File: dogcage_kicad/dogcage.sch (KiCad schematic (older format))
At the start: 10 parts, among them CON1 BARREL_JACK, M1 XBEE, P1 Servo, P2 Door Sensor, Q1 TIP120, SW1 SW_PUSH, U1 TEENSYLC, U2 LD1117S33TR

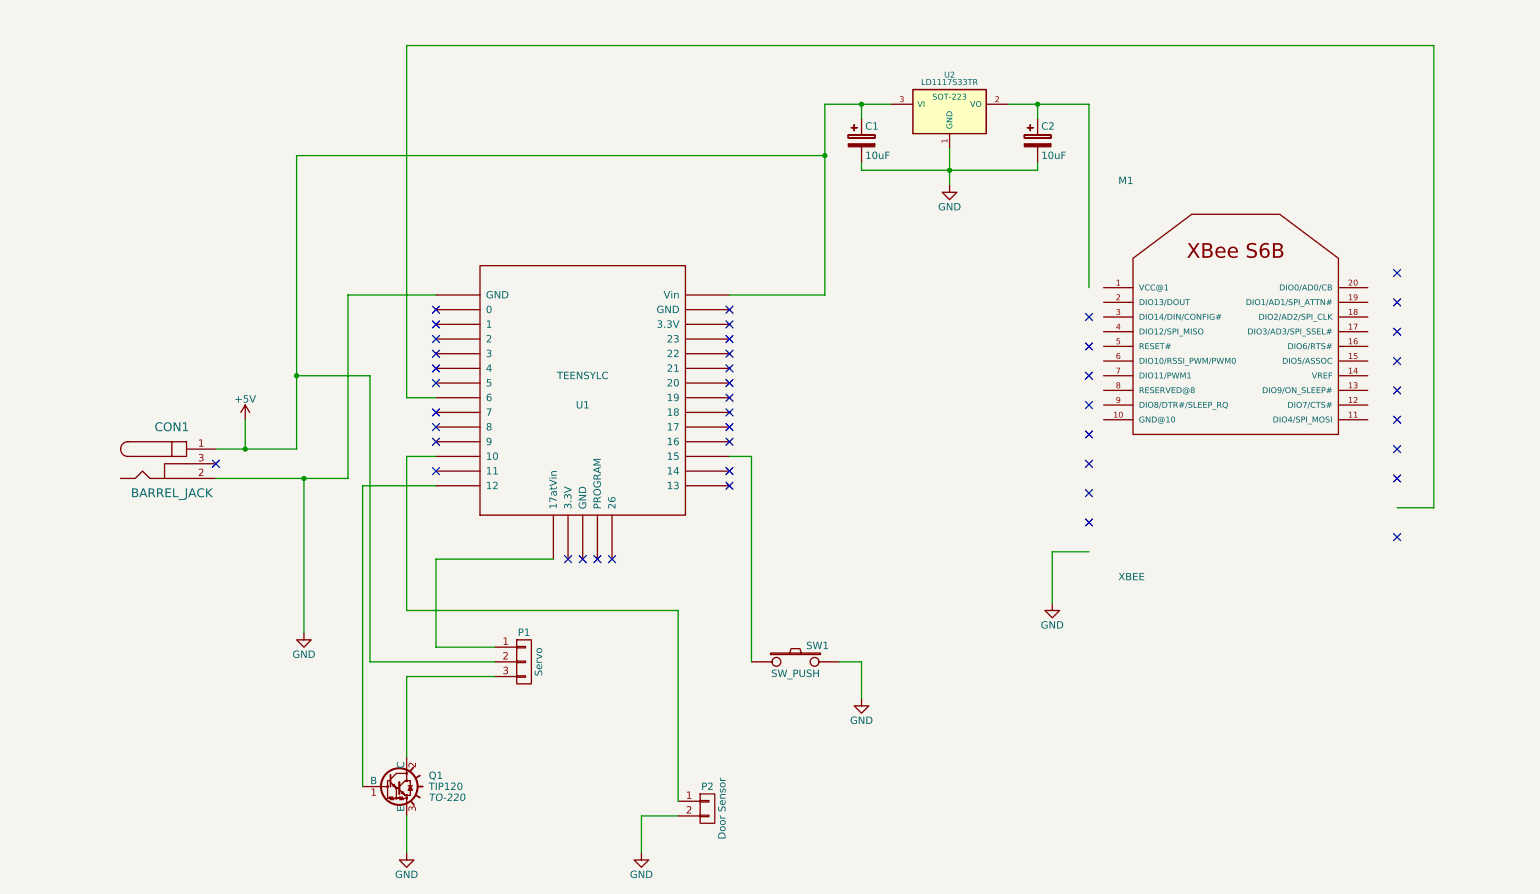
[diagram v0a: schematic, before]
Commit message: Cleaned up schematic and fixed ERC errors
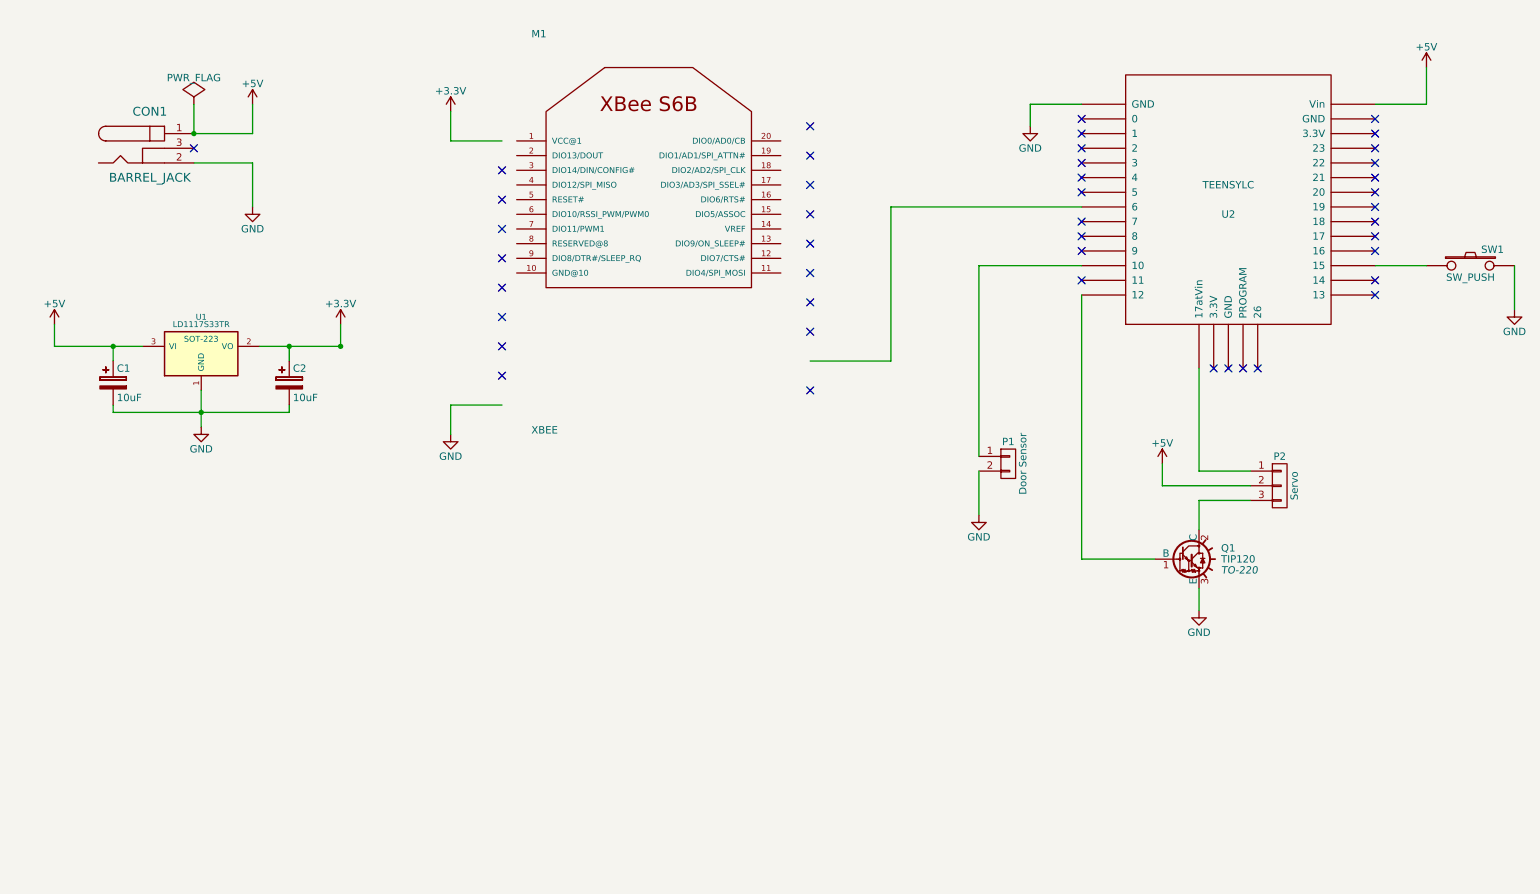
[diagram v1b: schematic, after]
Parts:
- renumbered P2 to P1, P1 to P2, U2 to U1, U1 to U2
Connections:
- net labels added: +3.3V
- wire segments 47 -> 40
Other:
- moved on the sheet: C1, C2, CON1, M1, P1, P2, Q1, SW1, U1, U2

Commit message: Added assoc LED and started on PCB
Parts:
- added D1: Assoc LED, symbol LED
- added R1: 330, symbol R
- CON1: footprint (none) -> Connect:BARREL_JACK
- P1: footprint (none) -> Pin_Headers:Pin_Header_Straight_1x02
- P2: footprint (none) -> Pin_Headers:Pin_Header_Straight_1x03
- Q1: footprint TO-220 -> Power_Integrations:TO-220
- SW1: footprint (none) -> Buttons_Switches_ThroughHole:SW_PUSH
- U1: footprint SOT-223 -> SMD_Packages:SOT-223
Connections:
- wire segments 40 -> 44
- no-connect marks 44 -> 43
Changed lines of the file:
@@
 F 0 "CON1" H 1550 1900 60  0000 C CNN
 F 1 "BARREL_JACK" H 1550 1450 60  0000 C CNN
-F 2 "" H 1550 1650 60  0000 C CNN
+F 2 "Connect:BARREL_JACK" H 1550 1650 60  0001 C CNN
 F 3 "" H 1550 1650 60  0000 C CNN
 	1    1550 1650
@@
 $EndComp
 $Comp
-L GND #PWR01
+L GND #PWR4
 U 1 1 553C44F5
 P 2250 2050
-F 0 "#PWR01" H 2250 1800 50  0001 C CNN
+F 0 "#PWR4" H 2250 1800 50  0001 C CNN
 F 1 "GND" H 2250 1900 50  0000 C CNN
 F 2 "" H 2250 2050 60  0000 C CNN
@@
 F 0 "P2" H 9250 4150 50  0000 C CNN
 F 1 "Servo" V 9350 3950 50  0000 C CNN
-F 2 "" H 9250 3950 60  0000 C CNN
+F 2 "Pin_Headers:Pin_Header_Straight_1x03" H 9250 3950 60  0001 C CNN
 F 3 "" H 9250 3950 60  0000 C CNN
 	1    9250 3950
@@
 $EndComp
 $Comp
-L GND #PWR02
+L GND #PWR12
 U 1 1 553C464F
 P 8700 4800
-F 0 "#PWR02" H 8700 4550 50  0001 C CNN
+F 0 "#PWR12" H 8700 4550 50  0001 C CNN
 F 1 "GND" H 8700 4650 50  0000 C CNN
 F 2 "" H 8700 4800 60  0000 C CNN
@@
 F 0 "SW1" H 10700 2560 50  0000 C CNN
 F 1 "SW_PUSH" H 10550 2370 50  0000 C CNN
-F 2 "" H 10550 2450 60  0000 C CNN
+F 2 "Buttons_Switches_ThroughHole:SW_PUSH" H 10550 2450 60  0001 C CNN
 F 3 "" H 10550 2450 60  0000 C CNN
 	1    10550 2450
@@
 	9900 2450 10250 2450
 $Comp
-L GND #PWR03
+L GND #PWR14
 U 1 1 553C47AE
 P 10850 2750
-F 0 "#PWR03" H 10850 2500 50  0001 C CNN
+F 0 "#PWR14" H 10850 2500 50  0001 C CNN
 F 1 "GND" H 10850 2600 50  0000 C CNN
 F 2 "" H 10850 2750 60  0000 C CNN
@@
 F 0 "P1" H 7400 3950 50  0000 C CNN
 F 1 "Door Sensor" V 7500 3800 50  0000 C CNN
-F 2 "" H 7400 3800 60  0000 C CNN
+F 2 "Pin_Headers:Pin_Header_Straight_1x02" H 7400 3800 60  0001 C CNN
 F 3 "" H 7400 3800 60  0000 C CNN
 	1    7400 3800
@@
 	7200 2450 7900 2450
 $Comp
-L GND #PWR04
+L GND #PWR9
 U 1 1 553C48BE
 P 7200 4150
-F 0 "#PWR04" H 7200 3900 50  0001 C CNN
+F 0 "#PWR9" H 7200 3900 50  0001 C CNN
 F 1 "GND" H 7200 4000 50  0000 C CNN
 F 2 "" H 7200 4150 60  0000 C CNN
@@
 F 0 "Q1" H 8850 4525 50  0000 L CNN
 F 1 "TIP120" H 8850 4450 50  0000 L CNN
-F 2 "TO-220" H 8850 4375 50  0000 L CIN
+F 2 "Power_Integrations:TO-220" H 8850 4375 50  0000 L CIN
 F 3 "" H 8600 4450 50  0000 L CNN
 	1    8600 4450
@@
 $EndComp
 $Comp
-L GND #PWR05
+L GND #PWR7
 U 1 1 553C50DC
 P 3600 3600
-F 0 "#PWR05" H 3600 3350 50  0001 C CNN
+F 0 "#PWR7" H 3600 3350 50  0001 C CNN
 F 1 "GND" H 3600 3450 50  0000 C CNN
 F 2 "" H 3600 3600 60  0000 C CNN
@@
 NoConn ~ 6050 2100
 NoConn ~ 6050 2300
-NoConn ~ 6050 2500
 NoConn ~ 6050 2700
 NoConn ~ 6050 2900
@@
 F 0 "U1" H 1900 3300 40  0000 C CNN
 F 1 "LD1117S33TR" H 1900 3250 40  0000 C CNN
-F 2 "SOT-223" H 1900 3150 40  0000 C CNN
+F 2 "SMD_Packages:SOT-223" H 1900 3150 40  0000 C CNN
 F 3 "" H 1900 3050 60  0000 C CNN
 	1    1900 3050
@@
 	2850 3000 2850 2850
 $Comp
-L GND #PWR06
+L GND #PWR2
 U 1 1 553C52E7
 P 1900 3550
-F 0 "#PWR06" H 1900 3300 50  0001 C CNN
+F 0 "#PWR2" H 1900 3300 50  0001 C CNN
 F 1 "GND" H 1900 3400 50  0000 C CNN
 F 2 "" H 1900 3550 60  0000 C CNN
@@
 F 0 "C1" H 1325 3350 50  0000 L CNN
 F 1 "10uF" H 1325 3150 50  0000 L CNN
-F 2 "" H 1338 3100 30  0000 C CNN
+F 2 "" H 1338 3100 30  0001 C CNN
 F 3 "" H 1300 3250 60  0000 C CNN
 	1    1300 3250
@@
 F 0 "C2" H 2525 3350 50  0000 L CNN
 F 1 "10uF" H 2525 3150 50  0000 L CNN
-F 2 "" H 2538 3100 30  0000 C CNN
+F 2 "" H 2538 3100 30  0001 C CNN
 F 3 "" H 2500 3250 60  0000 C CNN
 	1    2500 3250
@@
 Connection ~ 2500 3000
 $Comp
-L PWR_FLAG #FLG07
+L PWR_FLAG #FLG1
 U 1 1 553C5BFF
 P 1850 1350
-F 0 "#FLG07" H 1850 1445 50  0001 C CNN
+F 0 "#FLG1" H 1850 1445 50  0001 C CNN
 F 1 "PWR_FLAG" H 1850 1530 50  0000 C CNN
 F 2 "" H 1850 1350 60  0000 C CNN
@@
 	2250 1750 2250 2050
 $Comp
-L +5V #PWR08
+L +5V #PWR3
 U 1 1 553C5EEA
 P 2250 1350
-F 0 "#PWR08" H 2250 1200 50  0001 C CNN
+F 0 "#PWR3" H 2250 1200 50  0001 C CNN
 F 1 "+5V" H 2250 1490 50  0000 C CNN
 F 2 "" H 2250 1350 60  0000 C CNN
@@
 	2250 1550 2250 1350
 $Comp
-L +5V #PWR09
+L +5V #PWR11
 U 1 1 553C5FA1
 P 8450 3800
-F 0 "#PWR09" H 8450 3650 50  0001 C CNN
+F 0 "#PWR11" H 8450 3650 50  0001 C CNN
 F 1 "+5V" H 8450 3940 50  0000 C CNN
 F 2 "" H 8450 3800 60  0000 C CNN
@@
 	8450 3950 9050 3950
 $Comp
-L GND #PWR010
+L GND #PWR10
 U 1 1 553C6094
 P 7550 1500
-F 0 "#PWR010" H 7550 1250 50  0001 C CNN
+F 0 "#PWR10" H 7550 1250 50  0001 C CNN
 F 1 "GND" H 7550 1350 50  0000 C CNN
 F 2 "" H 7550 1500 60  0000 C CNN
@@
 	7550 1350 7550 1500
 $Comp
-L +5V #PWR011
+L +5V #PWR13
 U 1 1 553C6264
 P 10250 1100
-F 0 "#PWR011" H 10250 950 50  0001 C CNN
+F 0 "#PWR13" H 10250 950 50  0001 C CNN
 F 1 "+5V" H 10250 1240 50  0000 C CNN
 F 2 "" H 10250 1100 60  0000 C CNN
@@
 	10250 1350 9900 1350
 $Comp
-L +5V #PWR012
+L +5V #PWR1
 U 1 1 553C62D3
 P 900 2850
-F 0 "#PWR012" H 900 2700 50  0001 C CNN
+F 0 "#PWR1" H 900 2700 50  0001 C CNN
 F 1 "+5V" H 900 2990 50  0000 C CNN
 F 2 "" H 900 2850 60  0000 C CNN
@@
 Connection ~ 1300 3000
 $Comp
-L +3.3V #PWR013
+L +3.3V #PWR5
 U 1 1 553C6392
 P 2850 2850
-F 0 "#PWR013" H 2850 2700 50  0001 C CNN
+F 0 "#PWR5" H 2850 2700 50  0001 C CNN
 F 1 "+3.3V" H 2850 2990 50  0000 C CNN
 F 2 "" H 2850 2850 60  0000 C CNN
@@
 	7900 4450 8400 4450
 $Comp
-L +3.3V #PWR014
+L +3.3V #PWR6
 U 1 1 553C783D
 P 3600 1400
-F 0 "#PWR014" H 3600 1250 50  0001 C CNN
+F 0 "#PWR6" H 3600 1250 50  0001 C CNN
 F 1 "+3.3V" H 3600 1540 50  0000 C CNN
 F 2 "" H 3600 1400 60  0000 C CNN
@@
 Wire Wire Line
 	6600 2050 7900 2050
+$Comp
+L LED D1
+U 1 1 553D18EC
+P 6300 3900
+F 0 "D1" H 6300 4000 50  0000 C CNN
+F 1 "Assoc LED" H 6300 3800 50  0000 C CNN
+F 2 "" H 6300 3900 60  0000 C CNN
+F 3 "" H 6300 3900 60  0000 C CNN
+	1    6300 3900
+	0    1    1    0
+$EndComp
+$Comp
+L GND #PWR8
+U 1 1 553D1931
+P 6300 4150
+F 0 "#PWR8" H 6300 3900 50  0001 C CNN
+F 1 "GND" H 6300 4000 50  0000 C CNN
+F 2 "" H 6300 4150 60  0000 C CNN
+F 3 "" H 6300 4150 60  0000 C CNN
+	1    6300 4150
+	1    0    0    -1
+$EndComp
+$Comp
+L R R1
+U 1 1 553D19C7
+P 6300 3450
+F 0 "R1" V 6380 3450 50  0000 C CNN
+F 1 "330" V 6300 3450 50  0000 C CNN
+F 2 "" V 6230 3450 30  0000 C CNN
+F 3 "" H 6300 3450 30  0000 C CNN
+	1    6300 3450
+	1    0    0    -1
+$EndComp
+Wire Wire Line
+	6300 4150 6300 4100
+Wire Wire Line
+	6300 3600 6300 3700
+Wire Wire Line
+	6050 2500 6300 2500
+Wire Wire Line
+	6300 2500 6300 3300
 $EndSCHEMATC

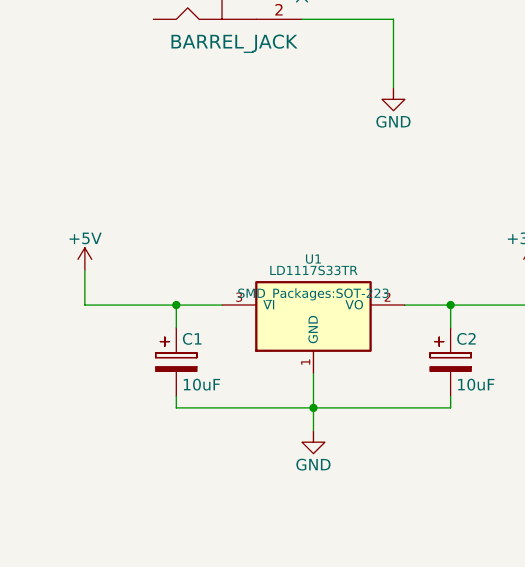
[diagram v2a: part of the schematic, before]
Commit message: Add protection diode to input power line
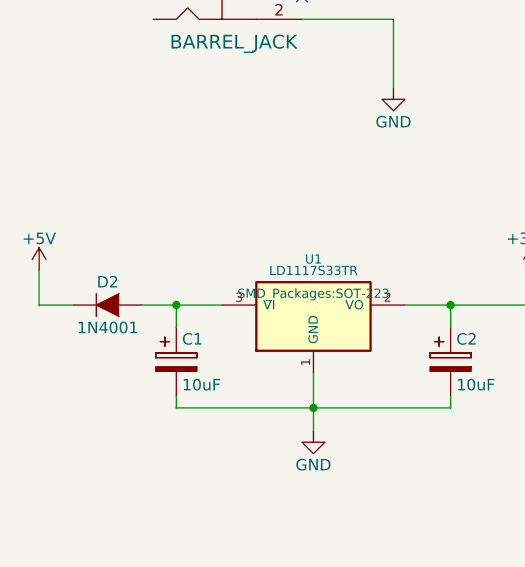
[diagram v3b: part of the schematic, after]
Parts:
- added D2: 1N4001, symbol D
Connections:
- wire segments 44 -> 45
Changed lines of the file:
@@
 $EndComp
 Wire Wire Line
-	900  3000 1500 3000
+	1150 3000 1500 3000
 Wire Wire Line
 	2300 3000 2850 3000
@@
 	2500 3450 2500 3400
 Wire Wire Line
-	1300 3100 1300 3000
+	1300 3000 1300 3100
 Wire Wire Line
 	2500 3100 2500 3000
@@
 L +5V #PWR1
 U 1 1 553C62D3
-P 900 2850
-F 0 "#PWR1" H 900 2700 50  0001 C CNN
-F 1 "+5V" H 900 2990 50  0000 C CNN
-F 2 "" H 900 2850 60  0000 C CNN
-F 3 "" H 900 2850 60  0000 C CNN
-	1    900  2850
-	1    0    0    -1
-$EndComp
-Wire Wire Line
-	900  2850 900  3000
+P 700 2850
+F 0 "#PWR1" H 700 2700 50  0001 C CNN
+F 1 "+5V" H 700 2990 50  0000 C CNN
+F 2 "" H 700 2850 60  0000 C CNN
+F 3 "" H 700 2850 60  0000 C CNN
+	1    700  2850
+	1    0    0    -1
+$EndComp
 Connection ~ 1300 3000
 $Comp
@@
 Wire Wire Line
 	6300 2500 6300 3300
+$Comp
+L D D2
+U 1 1 5541A2D5
+P 1000 3000
+F 0 "D2" H 1000 3100 50  0000 C CNN
+F 1 "1N4001" H 1000 2900 50  0000 C CNN
+F 2 "" H 1000 3000 60  0000 C CNN
+F 3 "" H 1000 3000 60  0000 C CNN
+	1    1000 3000
+	1    0    0    -1
+$EndComp
+Wire Wire Line
+	700  2850 700  3000
+Wire Wire Line
+	700  3000 850  3000
 $EndSCHEMATC

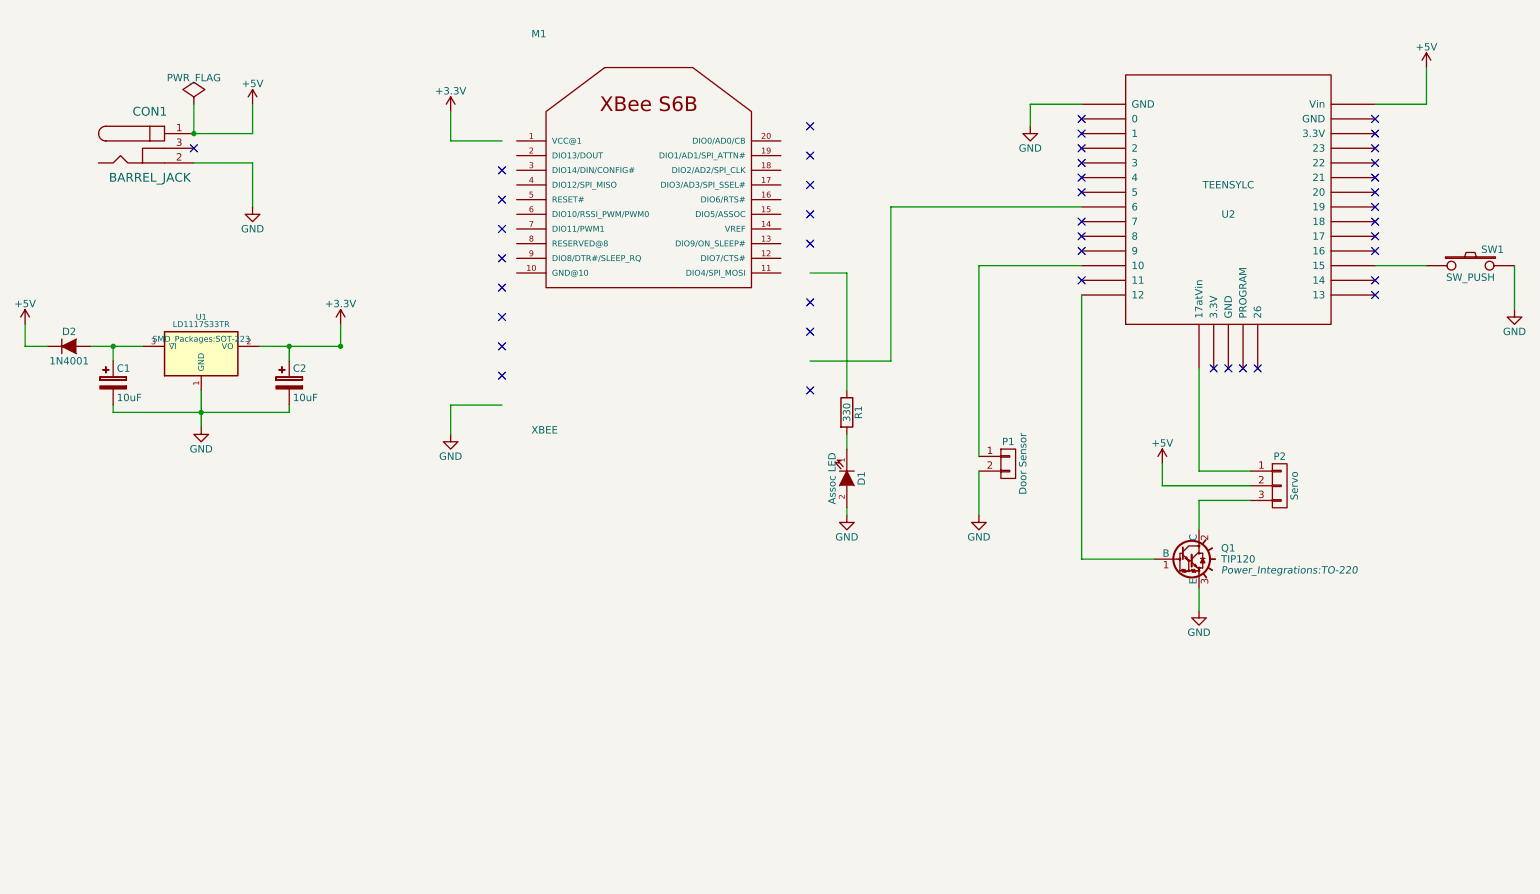
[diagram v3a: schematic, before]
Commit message: Added connectors to XBee and Teensy
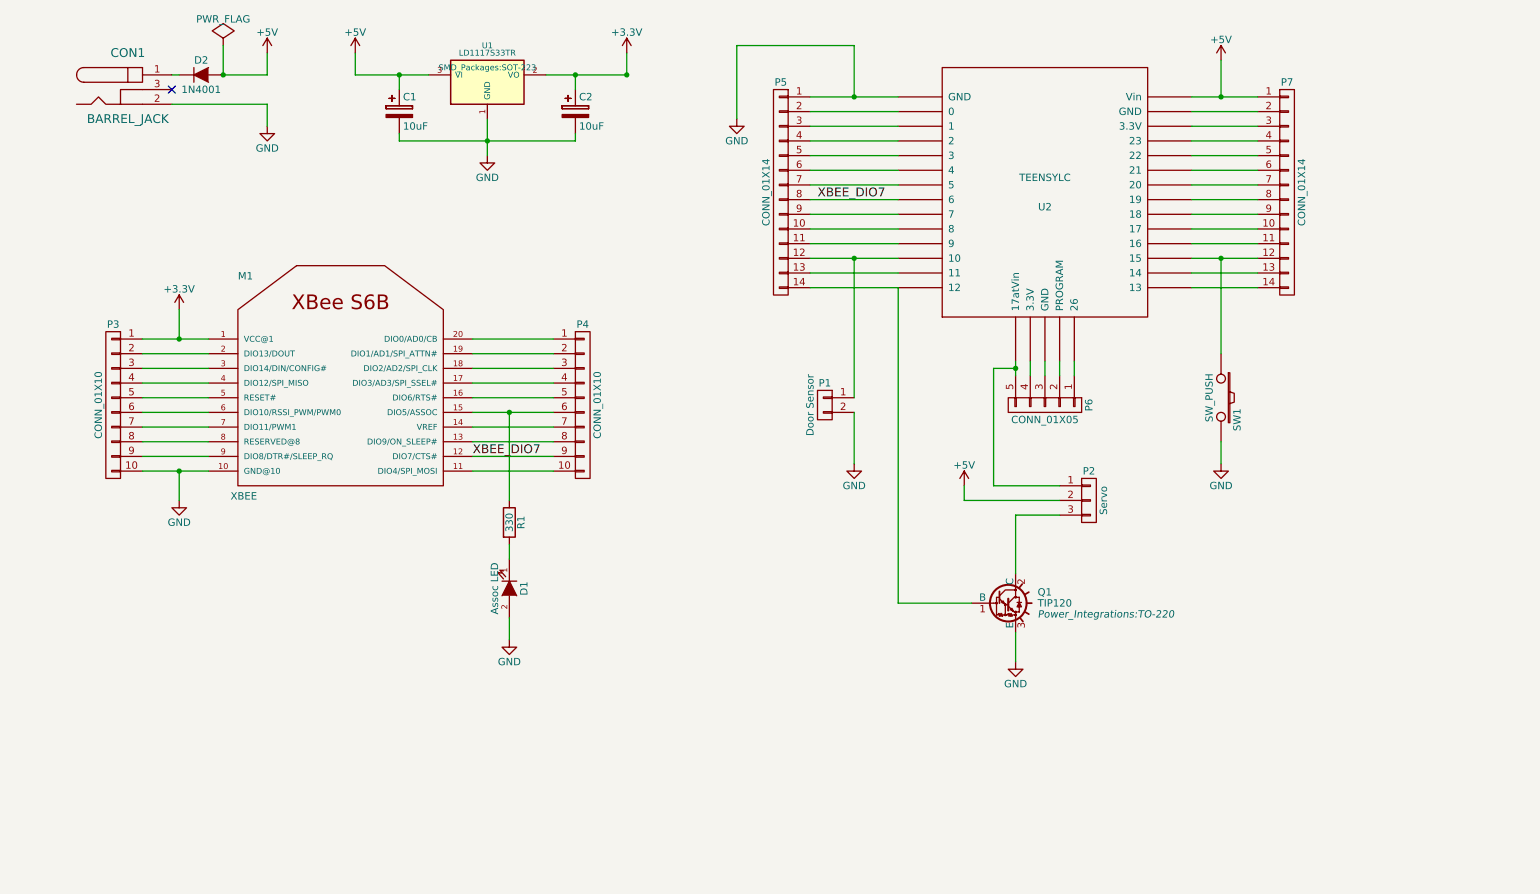
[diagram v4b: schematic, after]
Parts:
- added P3, P4: CONN_01X10, symbol CONN_01X10
- added P5, P7: CONN_01X14, symbol CONN_01X14
- added P6: CONN_01X05, symbol CONN_01X05
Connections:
- net labels added: XBEE_DIO7
- wire segments 45 -> 92
- no-connect marks 43 -> 1
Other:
- moved on the sheet: C1, C2, CON1, D1, D2, P1, P2, Q1, R1, SW1, U1, U2
